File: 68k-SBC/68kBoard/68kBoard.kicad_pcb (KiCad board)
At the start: 2 copper layers, 154.9 x 134.6 mm, 65 parts, among them J1 ADBUS, J2 SIGBUS, J3 Barrel_Jack, J4 Serial1, J5 Serial2, Q1 Q_NMOS_DGS, SW1 RESET, U1 74HC14, U10 HM628512, U11 68681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

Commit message: Mostly done 68k board design
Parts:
- D2: renamed from OP5; value LED -> OP5
- D3: renamed from OP7; value LED -> OP7
- D4: renamed from OP4; value LED -> OP4
- D5: renamed from OP6; value LED -> OP6
- SW2: renamed from IP4; value SW_Push -> IP4
- SW3: renamed from IP5; value SW_Push -> IP5
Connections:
- net IACK renamed SIACK
- J2 pad 19: Net-(J2-Pad19) -> ROMSEL
- J2 pad 21: ROMSEL -> 0SEL
- J2 pad 23: 0SEL -> RAMSEL
- J2 pad 25: RAMSEL -> 2SEL
- J2 pad 27: 2SEL -> 3SEL
- J2 pad 29: 3SEL -> 4SEL
- J2 pad 30: OP2 -> SIRQ
- J2 pad 31: 4SEL -> 5SEL
- J2 pad 32: OP3 -> OP2
- J2 pad 33: 5SEL -> 6SEL
- J2 pad 34: IP2 -> OP3
- J2 pad 35: 6SEL -> IOSEL
- J2 pad 36: IP3 -> IP2
- J2 pad 37: IOSEL -> CLK
- J2 pad 38: CLK -> IP3
- U11 pad 21: IPL0 -> SIRQ
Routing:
- net SIRQ: track 0.00 -> 202.2 mm, vias 0 -> 1
- net IPL0: track 193.0 -> 173.3 mm, vias 3 -> 2
- net D7: track 278.8 -> 284.3 mm
- net D5: track 274.8 -> 278.7 mm
- net IP2: track 226.3 -> 222.7 mm
- net IP3: track 222.9 -> 219.8 mm
- net OP3: track 204.8 -> 201.9 mm
- net OP2: track 217.9 -> 215.2 mm
- net D6: track 276.5 -> 273.9 mm
- net CLK: track 196.3 -> 193.7 mm
- net Net-(D3-Pad1): track 46.5 -> 44.2 mm
- net D3: track 298.3 -> 300.6 mm
- net 4SEL: track 20.5 -> 22.3 mm
- net SIACK: track 241.2 -> 242.9 mm
- net D4: track 289.2 -> 287.5 mm
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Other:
- board text added: "SIACK"
- board text added: "SIRQ"
- board text removed: "IACK"

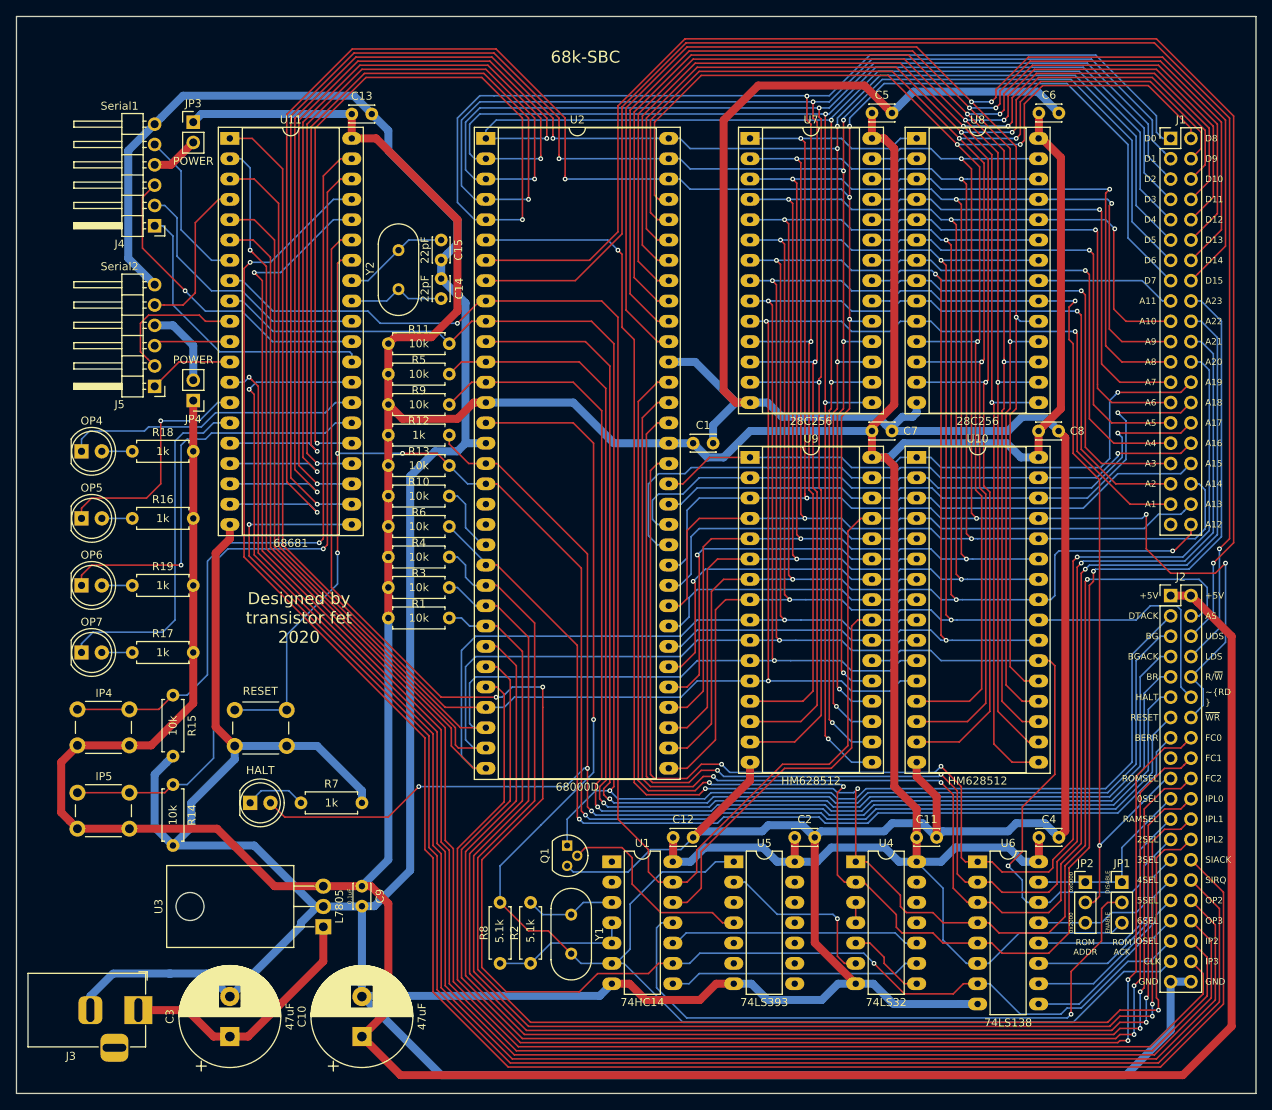
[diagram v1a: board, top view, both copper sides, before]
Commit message: Fixed some issues after testing with the 68681 chips
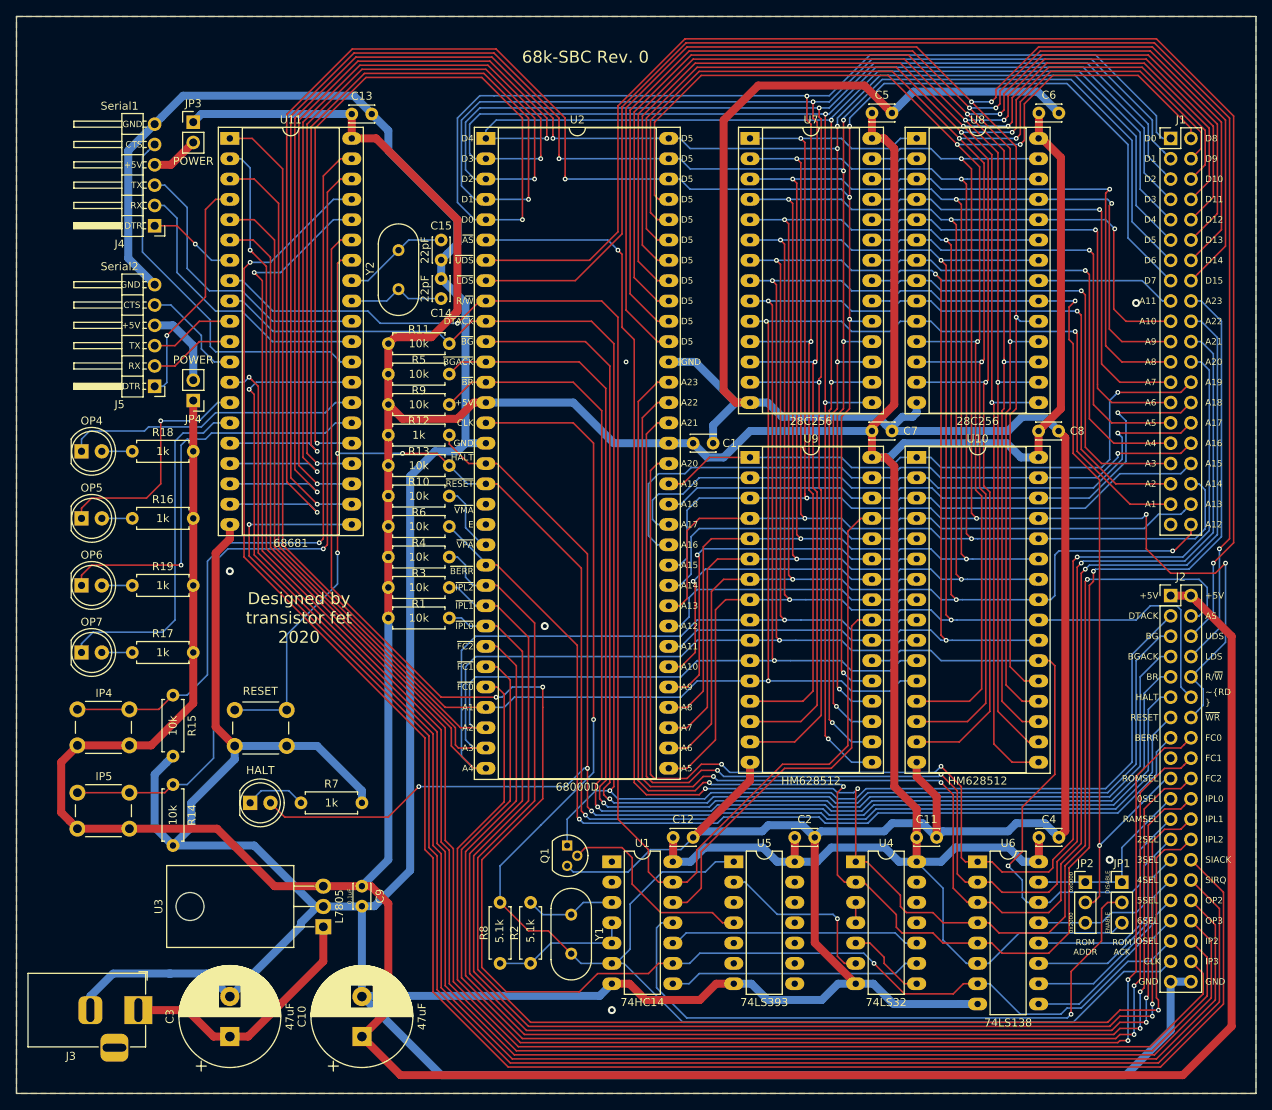
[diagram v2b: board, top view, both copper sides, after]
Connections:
- U11 pad 10: Net-(J5-Pad2) -> Net-(J5-Pad3)
- U11 pad 11: Net-(J5-Pad3) -> Net-(J5-Pad2)
- U11 pad 12: Net-(J5-Pad1) -> Net-(J5-Pad5)
- U11 pad 29: Net-(J4-Pad1) -> Net-(J4-Pad5)
- U11 pad 30: Net-(J4-Pad3) -> Net-(J4-Pad2)
- U11 pad 31: Net-(J4-Pad2) -> Net-(J4-Pad3)
- U11 pad 4: Net-(J5-Pad5) -> Net-(J5-Pad1)
- U11 pad 7: Net-(J4-Pad5) -> Net-(J4-Pad1)
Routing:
- net Net-(J4-Pad5): track 19.7 -> 47.9 mm
- net Net-(J4-Pad1): track 37.3 -> 11.2 mm, vias 0 -> 1
- net Net-(J5-Pad1): track 10.7 -> 28.9 mm, vias 0 -> 1
- net Net-(J5-Pad2): track 18.0 -> 10.7 mm
- net Net-(J5-Pad5): track 20.0 -> 13.3 mm
- net Net-(J4-Pad3): track 39.5 -> 36.2 mm, vias 1 -> 0
- net Net-(J4-Pad2): track 33.5 -> 35.7 mm
- net Net-(J5-Pad3): track 9.61 -> 10.7 mm
- net D9: track 191.0 -> 192.0 mm
- net D8: track 179.5 -> 180.6 mm
- net D15: track 221.7 -> 222.8 mm
- net D13: track 213.1 -> 214.1 mm
- net D12: track 208.3 -> 209.4 mm
- net D11: track 205.5 -> 206.5 mm
- net D14: track 217.4 -> 218.4 mm
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- added copper zone on B.Cu, net GND
- added copper zone on F.Cu, net GND
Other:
- board text added: "68k-SBC Rev. 0"
- board text added: "CTS"
- board text added: "DTR"
- board text added: "E"
- board text added: "RX"
- board text added: "TX"
- board text added: "~AS"
- board text added: "~BERR"
- board text added: "~BG"
- board text added: "~BGACK"
- board text added: "~BR"
- board text added: "~DTACK"
- board text added: "~FC0"
- board text added: "~FC1"
- board text added: "~FC2"
- board text added: "~HALT"
- board text added: "~IPL0"
- board text added: "~IPL1"
- board text added: "~IPL2"
- board text added: "~LDS"
- board text added: "~RESET"
- board text added: "~UDS"
- board text added: "~VMA"
- board text added: "~VPA"
- board text removed: "68k-SBC"

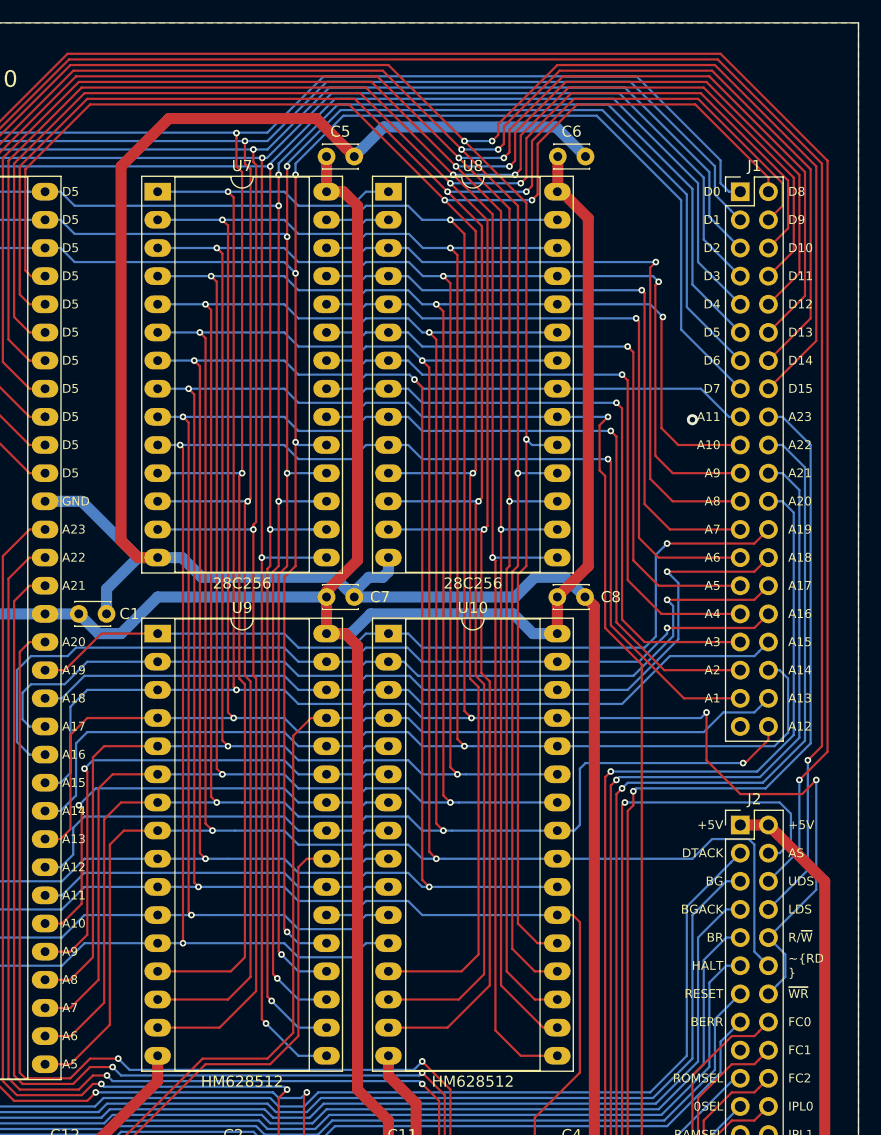
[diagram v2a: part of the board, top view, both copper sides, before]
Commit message: Reordered address and data buses for easier connection to arduino
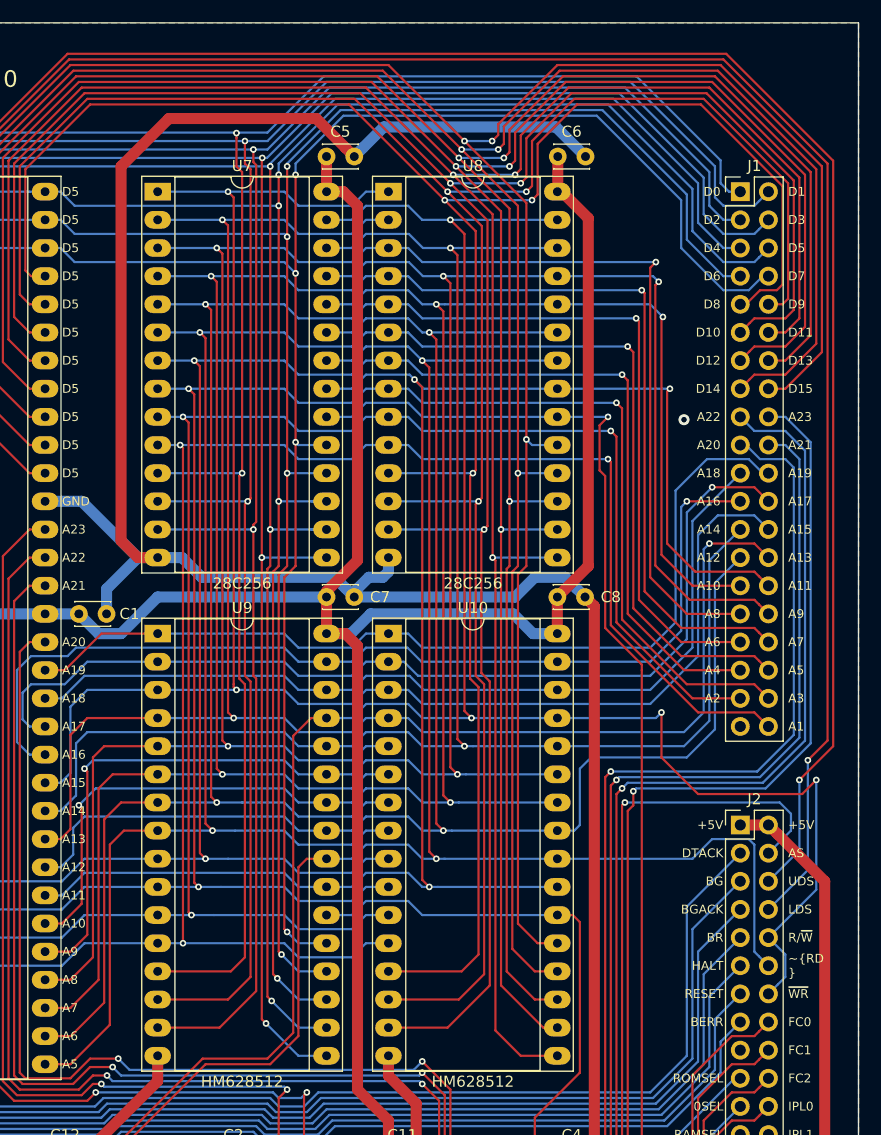
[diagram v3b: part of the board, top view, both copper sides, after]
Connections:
- J1 pad 10: D12 -> D9
- J1 pad 11: D5 -> D10
- J1 pad 12: D13 -> D11
- J1 pad 13: D6 -> D12
- J1 pad 14: D14 -> D13
- J1 pad 15: D7 -> D14
- J1 pad 17: A11 -> A22
- J1 pad 19: A10 -> A20
- J1 pad 2: D8 -> D1
- J1 pad 20: A22 -> A21
- J1 pad 21: A9 -> A18
- J1 pad 22: A21 -> A19
- J1 pad 23: A8 -> A16
- J1 pad 24: A20 -> A17
- J1 pad 25: A7 -> A14
- J1 pad 26: A19 -> A15
- J1 pad 27: A6 -> A12
- J1 pad 28: A18 -> A13
- J1 pad 29: A5 -> A10
- J1 pad 3: D1 -> D2
- J1 pad 30: A17 -> A11
- J1 pad 31: A4 -> A8
- J1 pad 32: A16 -> A9
- J1 pad 33: A3 -> A6
- J1 pad 34: A15 -> A7
- J1 pad 35: A2 -> A4
- J1 pad 36: A14 -> A5
- J1 pad 37: A1 -> A2
- J1 pad 38: A13 -> A3
- J1 pad 4: D9 -> D3
- J1 pad 40: A12 -> A1
- J1 pad 5: D2 -> D4
- J1 pad 6: D10 -> D5
- J1 pad 7: D3 -> D6
- J1 pad 8: D11 -> D7
- J1 pad 9: D4 -> D8
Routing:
- net A11: track 134.3 -> 151.7 mm, vias 2 -> 3
- net A13: track 144.9 -> 159.8 mm, vias 2 -> 3
- net D8: track 180.6 -> 194.3 mm
- net A9: track 165.0 -> 178.6 mm
- net A10: track 153.8 -> 165.8 mm
- net A15: track 143.3 -> 155.0 mm
- net A7: track 170.5 -> 181.9 mm
- net D10: track 202.3 -> 213.3 mm
- net A12: track 145.1 -> 155.9 mm, vias 3 -> 2
- net A8: track 172.0 -> 181.4 mm
- net D9: track 192.0 -> 201.1 mm
- net D12: track 209.4 -> 217.9 mm
- net A5: track 169.8 -> 178.1 mm
- net A17: track 80.8 -> 89.0 mm
- net A16: track 81.8 -> 89.7 mm
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
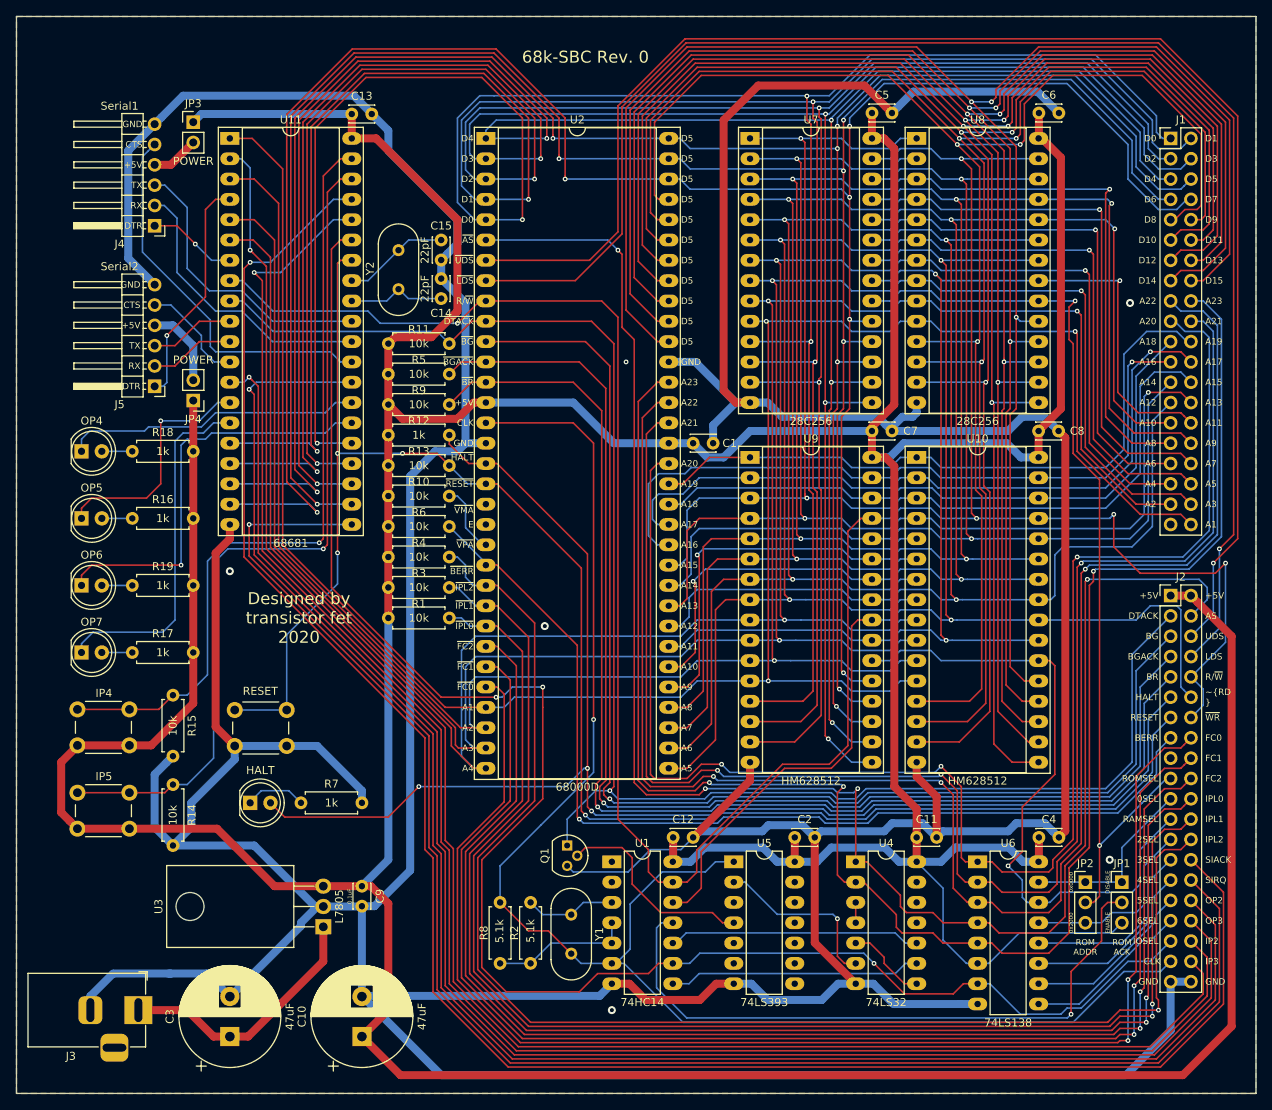
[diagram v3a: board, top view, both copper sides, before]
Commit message: Finalized 68kBoard and 68kBoardSupervisorShield
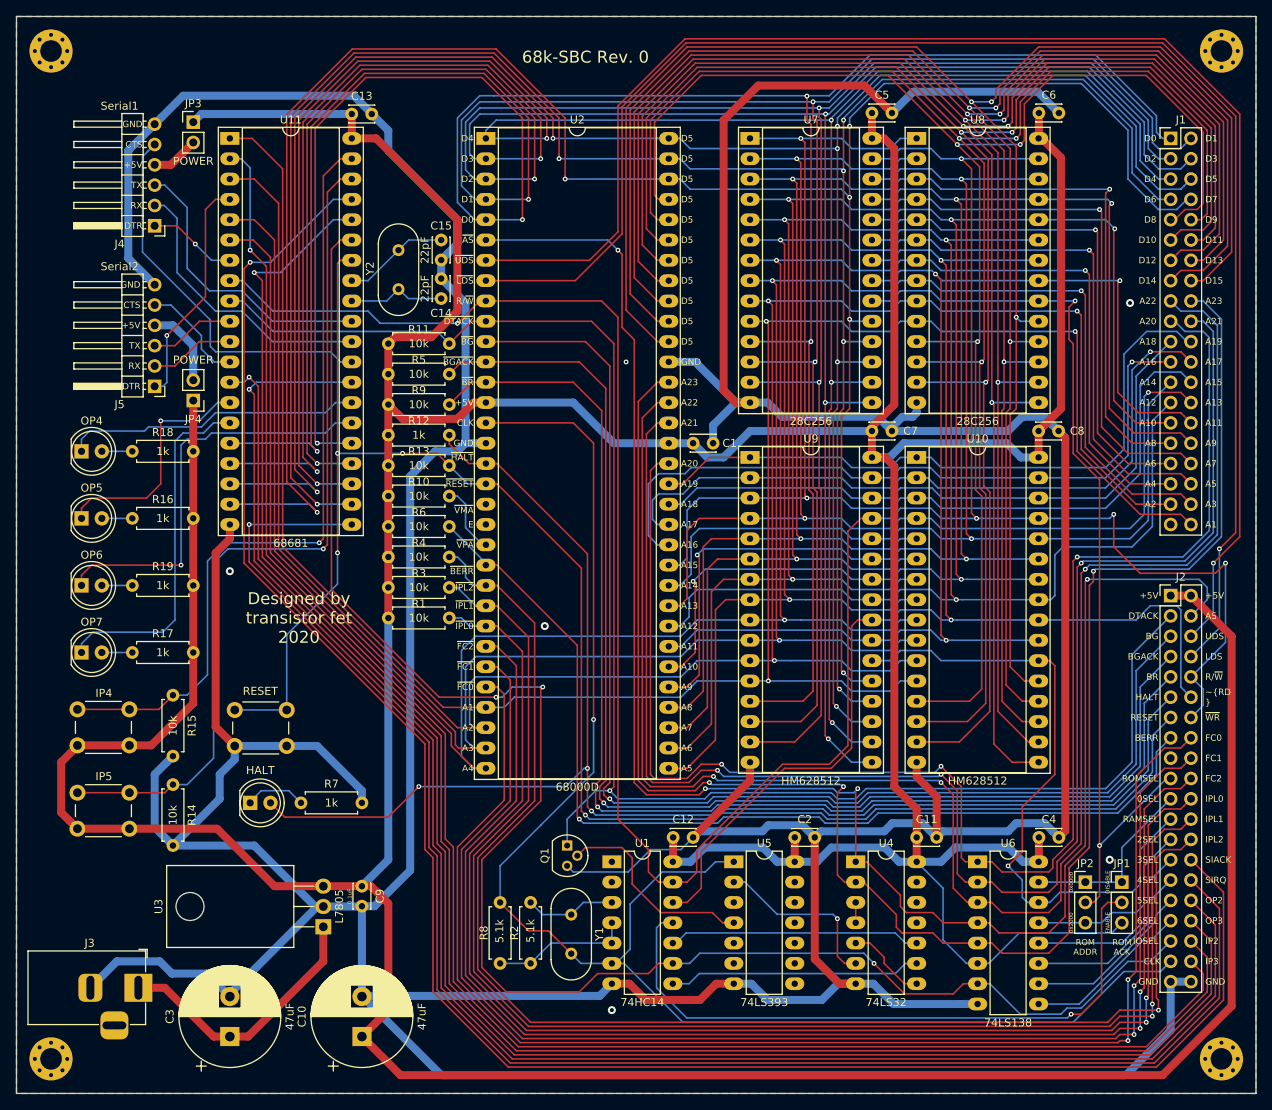
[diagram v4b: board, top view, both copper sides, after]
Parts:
- added ?: , MountingHole:MountingHole_2.7mm_Pad_Via, F.Cu at (60.2, 29.7)
- added ?: , MountingHole:MountingHole_2.7mm_Pad_Via, F.Cu at (60.2, 155.7)
- added ?: , MountingHole:MountingHole_2.7mm_Pad_Via, F.Cu at (206.5, 155.7)
- added ?: , MountingHole:MountingHole_2.7mm_Pad_Via, F.Cu at (206.5, 29.7)
- moved J3 2.79 mm to (71.1, 146.8)
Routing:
- net +5V: track 764.1 -> 762.7 mm
- net Net-(C3-Pad1): track 32.7 -> 33.8 mm
- net D7: track 279.3 -> 280.4 mm
- net D6: track 267.1 -> 268.0 mm
- net Net-(JP1-Pad2): track 81.0 -> 81.7 mm
- net D5: track 276.3 -> 277.1 mm
- net D4: track 283.3 -> 283.9 mm
- net D14: track 224.4 -> 224.9 mm
- net D11: track 213.2 -> 213.7 mm
- net D8: track 194.3 -> 194.8 mm
- net UDS: track 186.1 -> 186.6 mm
- net LDS: track 188.5 -> 189.0 mm
- net D15: track 224.4 -> 224.9 mm
- net D13: track 218.3 -> 218.8 mm
- net D12: track 217.9 -> 218.4 mm
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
